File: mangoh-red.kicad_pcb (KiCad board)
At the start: 6 copper layers, 70 x 61.8 mm, 256 parts, among them CN301 uFL, CN302 uFL, CN303 uFL, CN304 USB_A, CN305 USB_B_Micro, CN307 Conn_02x13_Odd_Even, CN312 Conn_02x03_Odd_Even, CN801 USB_B_Micro, CN802 Conn_01x02, CN804 Conn_01x03, J200 CF3-Socket, Q312 NSBC114YDP6T5G, Q400 NSBC114YDP6T5G, Q600 PDTC115EM, SW401 Conn_02x08_Counter_Clockwise, U1004 SX1509BIULTRT, U1005 TPS61253YFFR, U1007 24AA32AF-I-MNY, U301 FT230XQ-R, U306 FXMA108BQX, U307 FXMA108BQX, U400 NCP303LSN30T1G, U402 74AUP1G08GM, U404 TCA9546APWR, U600 XC6223H29B9R-G, U610 TXS02612ZQSR, U701 USB3503A-1-GL-TR, U702 MIC2026-1YM, U704 BMI160, U800 BQ24296RGER, U801 LTC2942IDCB_TRMPBF, U901 TPS62420DRC, U903 XC6221A182MR

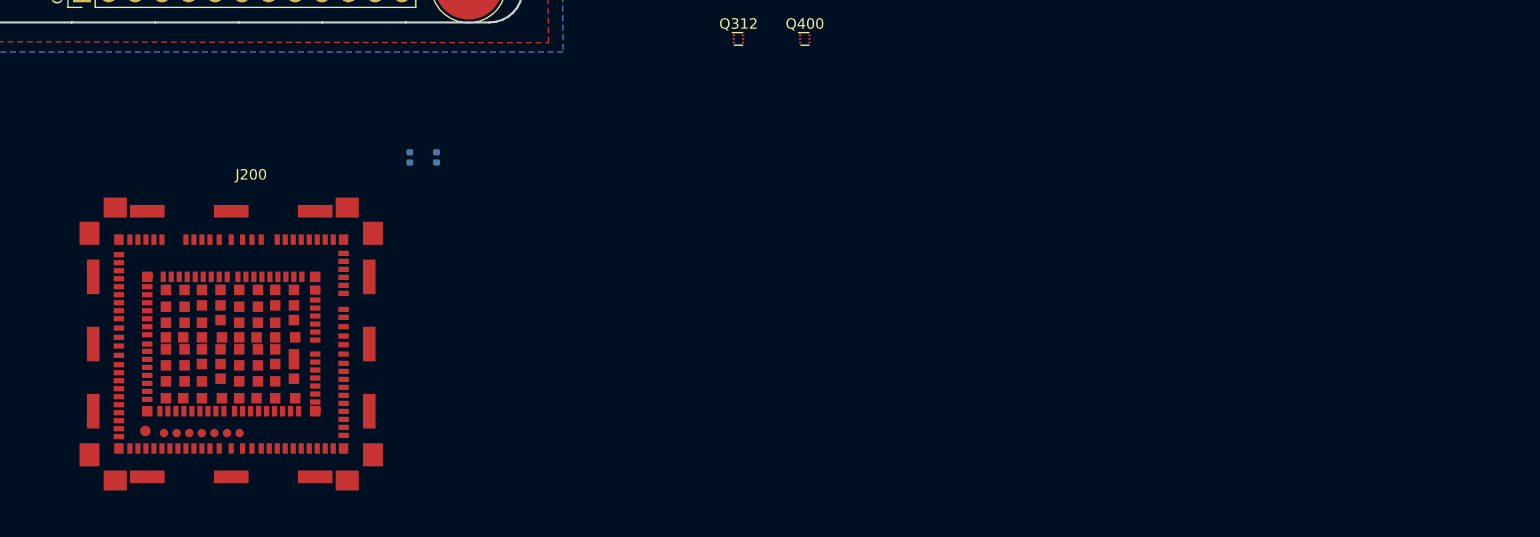
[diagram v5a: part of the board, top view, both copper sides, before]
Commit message: Change footprint of CF3 socket to use the one generated by SnapEDA.
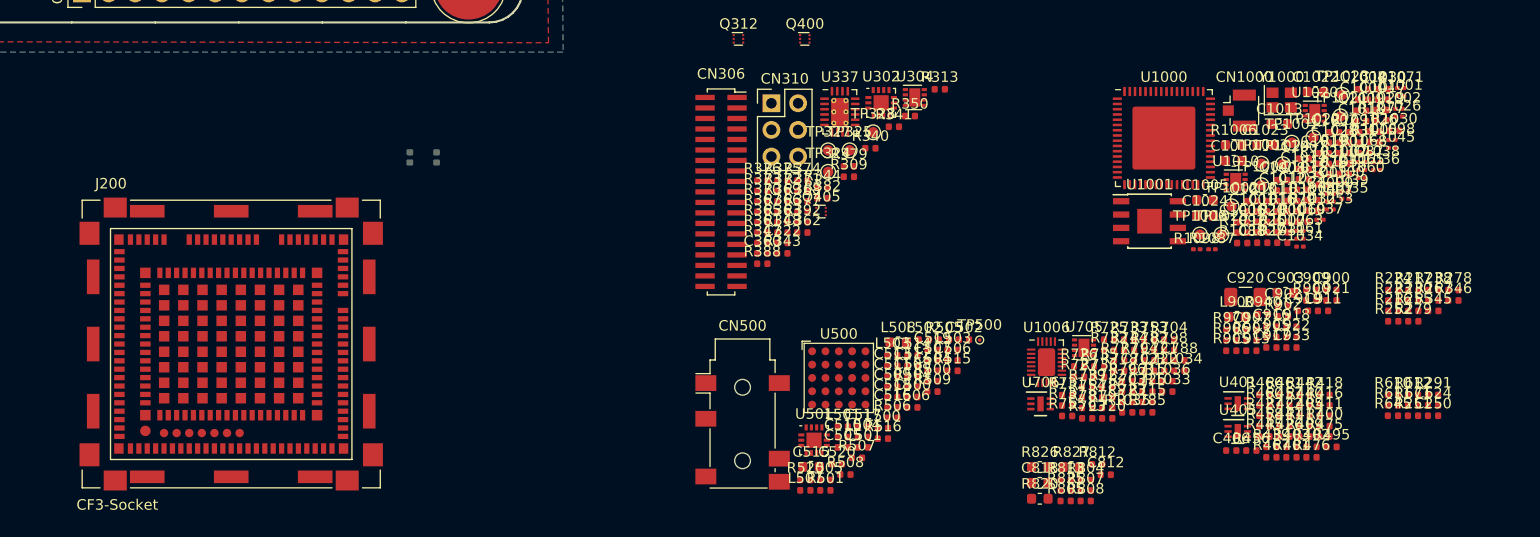
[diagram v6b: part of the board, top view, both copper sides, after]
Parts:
- added C1000: 100n, Capacitor_SMD:C_0402_1005Metric, F.Cu at (269.9, 124.7)
- added C1001: 470n, Capacitor_SMD:C_0402_1005Metric, F.Cu at (259.3, 135.3)
- added C1002: 10p, Capacitor_SMD:C_0402_1005Metric, F.Cu at (267.1, 127.8)
- added C1003: 100n, Capacitor_SMD:C_0402_1005Metric, F.Cu at (259.3, 134.3)
- added C1004: 470n, Capacitor_SMD:C_0402_1005Metric, F.Cu at (269.9, 123.7)
- added C1005: 10u, Capacitor_SMD:C_0603_1608Metric, F.Cu at (254.8, 134.2)
- added C1006: 100p, Capacitor_SMD:C_0402_1005Metric, F.Cu at (258.4, 136.4)
- added C1007: 100n, Capacitor_SMD:C_0402_1005Metric, F.Cu at (264.2, 130.3)
- added C1008: 4.7u, Capacitor_SMD:C_0402_1005Metric, F.Cu at (262.2, 132.3)
- added C1009: 4.7u, Capacitor_SMD:C_0402_1005Metric, F.Cu at (269.7, 125.7)
- added C1010: 2.2u, Capacitor_SMD:C_0603_1608Metric, F.Cu at (257.6, 130.5)
- added C1011: 1u, Capacitor_SMD:C_0402_1005Metric, F.Cu at (261.2, 134.3)
- added C1012: 100n, Capacitor_SMD:C_0402_1005Metric, F.Cu at (262.2, 133.3)
- added C1013: 10u, Capacitor_SMD:C_0603_1608Metric, F.Cu at (261.9, 127.0)
- added C1014: 100n, Capacitor_SMD:C_0402_1005Metric, F.Cu at (264.2, 131.3)
- added C1015: 470p, Capacitor_SMD:C_0402_1005Metric, F.Cu at (264.2, 132.3)
- added C1016: 1u, Capacitor_SMD:C_0402_1005Metric, F.Cu at (261.2, 135.3)
- added C1017: 10u, Capacitor_SMD:C_0402_1005Metric, F.Cu at (271.8, 124.7)
- added C1018: 1u, Capacitor_SMD:C_0402_1005Metric, F.Cu at (269.7, 126.7)
- added C1019: 100p, Capacitor_SMD:C_0402_1005Metric, F.Cu at (266.1, 129.8)
- added C1020: 100n, Capacitor_SMD:C_0402_1005Metric, F.Cu at (260.3, 136.3)
- added C1021: 1u, Capacitor_SMD:C_0402_1005Metric, F.Cu at (266.1, 130.8)
- added C1022: 2.2u, Capacitor_SMD:C_0603_1608Metric, F.Cu at (265.4, 123.9)
- added C1023: 2.2u, Capacitor_SMD:C_0603_1608Metric, F.Cu at (260.6, 129.0)
- added C1024: 2.2u, Capacitor_SMD:C_0603_1608Metric, F.Cu at (254.8, 135.7)
- added C1025: 4.7u, Capacitor_SMD:C_0402_1005Metric, F.Cu at (260.3, 137.3)
- added C1026: 100p, Capacitor_SMD:C_0402_1005Metric, F.Cu at (270.9, 127.7)
- added C1027: 10p, Capacitor_SMD:C_0402_1005Metric, F.Cu at (260.3, 138.3)
- added C1028: 10p, Capacitor_SMD:C_0402_1005Metric, F.Cu at (267.1, 128.8)
- added C1029: 10p, Capacitor_SMD:C_0402_1005Metric, F.Cu at (271.6, 125.7)
- added C1030: 100p, Capacitor_SMD:C_0402_1005Metric, F.Cu at (271.8, 123.7)
- added C1031: 10p, Capacitor_SMD:C_0402_1005Metric, F.Cu at (269.0, 128.8)
- added C1032: 1u, Capacitor_SMD:C_0402_1005Metric, F.Cu at (264.1, 133.3)
- added C1033: 100p, Capacitor_SMD:C_0402_1005Metric, F.Cu at (263.1, 134.3)
- added C1034: 1p, Capacitor_SMD:C_0201_0603Metric, F.Cu at (263.9, 138.7)
- added C1035: 1.5p, Capacitor_SMD:C_0201_0603Metric, F.Cu at (268.2, 134.1)
- added C1036: 1.5p, Capacitor_SMD:C_0201_0603Metric, F.Cu at (271.2, 131.4)
- added C1037: 1.8p, Capacitor_SMD:C_0201_0603Metric, F.Cu at (265.8, 136.1)
- added C1038: 1.8p, Capacitor_SMD:C_0201_0603Metric, F.Cu at (271.2, 130.6)
- added C1039: 1.5p, Capacitor_SMD:C_0201_0603Metric, F.Cu at (268.2, 133.4)
- added C1045: 10p, Capacitor_SMD:C_0201_0603Metric, F.Cu at (272.6, 129.3)
- added C1053: 1.5p, Capacitor_SMD:C_0201_0603Metric, F.Cu at (266.7, 135.1)
- added C1060: 2.7p, Capacitor_SMD:C_0201_0603Metric, F.Cu at (269.7, 132.1)
- added C1061: 100p, Capacitor_SMD:C_0201_0603Metric, F.Cu at (263.9, 137.9)
- added C1063: 10p, Capacitor_SMD:C_0201_0603Metric, F.Cu at (263.9, 137.2)
- added C1065: 1.5p, Capacitor_SMD:C_0201_0603Metric, F.Cu at (269.7, 131.4)
- added C1087: 2.2p, Capacitor_SMD:C_0201_0603Metric, F.Cu at (266.7, 134.4)
- added C1098: 10p, Capacitor_SMD:C_0201_0603Metric, F.Cu at (272.6, 128.5)
- added C1099: 10p, Capacitor_SMD:C_0201_0603Metric, F.Cu at (266.7, 133.6)
- added C1100: 10p, Capacitor_SMD:C_0201_0603Metric, F.Cu at (267.8, 132.6)
- added C250: 1n, Capacitor_SMD:C_0402_1005Metric, F.Cu at (276.5, 154.8)
- added C322: 100n, Capacitor_SMD:C_0402_1005Metric, F.Cu at (214.6, 138.3)
- added C360: 100n, Capacitor_SMD:C_0402_1005Metric, F.Cu at (212.6, 139.3)
- added C362: 100n, Capacitor_SMD:C_0402_1005Metric, F.Cu at (216.5, 137.3)
- added C405: 100n, Capacitor_SMD:C_0402_1005Metric, F.Cu at (264.3, 154.8)
- added C406: 100n, Capacitor_SMD:C_0402_1005Metric, F.Cu at (257.3, 158.1)
- added C500: 100p, Capacitor_SMD:C_0402_1005Metric, F.Cu at (226.9, 153.0)
- added C501: 100p, Capacitor_SMD:C_0402_1005Metric, F.Cu at (222.2, 157.8)
- added C502: 100p, Capacitor_SMD:C_0402_1005Metric, F.Cu at (231.9, 147.5)
- added C503: 1u, Capacitor_SMD:C_0402_1005Metric, F.Cu at (230.8, 148.5)
- added C504: 1u, Capacitor_SMD:C_0402_1005Metric, F.Cu at (228.9, 150.5)
- added C505: 100p, Capacitor_SMD:C_0402_1005Metric, F.Cu at (220.3, 157.8)
- added C506: 100p, Capacitor_SMD:C_0402_1005Metric, F.Cu at (230.8, 149.5)
- added C507: 22p, Capacitor_SMD:C_0402_1005Metric, F.Cu at (228.9, 149.5)
- added C508: 22p, Capacitor_SMD:C_0402_1005Metric, F.Cu at (226.9, 151.0)
- added C509: 4.7u, Capacitor_SMD:C_0402_1005Metric, F.Cu at (225.0, 152.0)
- added C510: 100p, Capacitor_SMD:C_0402_1005Metric, F.Cu at (220.3, 156.8)
- added C511: 100p, Capacitor_SMD:C_0402_1005Metric, F.Cu at (225.0, 151.0)
- added C512: 4.7u, Capacitor_SMD:C_0402_1005Metric, F.Cu at (226.9, 150.0)
- added C513: 4.7u, Capacitor_SMD:C_0402_1005Metric, F.Cu at (225.0, 150.0)
- added C514: 4.7u, Capacitor_SMD:C_0402_1005Metric, F.Cu at (226.9, 149.0)
- added C515: 2.2u, Capacitor_SMD:C_0603_1608Metric, F.Cu at (217.3, 159.7)
- added C516: 100p, Capacitor_SMD:C_0402_1005Metric, F.Cu at (225.0, 154.0)
- added C517: 100n, Capacitor_SMD:C_0402_1005Metric, F.Cu at (222.2, 155.8)
- added C518: 100n, Capacitor_SMD:C_0402_1005Metric, F.Cu at (225.0, 153.0)
- added C519: 4.7u, Capacitor_SMD:C_0402_1005Metric, F.Cu at (228.9, 148.5)
- added C520: 100n, Capacitor_SMD:C_0402_1005Metric, F.Cu at (219.8, 159.4)
- added C624: 100n, Capacitor_SMD:C_0402_1005Metric, F.Cu at (276.5, 153.8)
- added C702: 100n, Capacitor_SMD:C_0402_1005Metric, F.Cu at (248.6, 150.5)
- added C715: 100n, Capacitor_SMD:C_0402_1005Metric, F.Cu at (249.3, 151.5)
- added C720: 100n, Capacitor_SMD:C_0402_1005Metric, F.Cu at (245.5, 155.0)
- added C721: 100n, Capacitor_SMD:C_0402_1005Metric, F.Cu at (250.5, 149.5)
- added C722: 100n, Capacitor_SMD:C_0402_1005Metric, F.Cu at (250.5, 150.5)
- added C723: 100n, Capacitor_SMD:C_0402_1005Metric, F.Cu at (247.4, 153.5)
- added C725: 100n, Capacitor_SMD:C_0402_1005Metric, F.Cu at (249.3, 152.5)
- added C788: 4.7u, Capacitor_SMD:C_0402_1005Metric, F.Cu at (252.4, 149.5)
- added C812: 10u, Capacitor_SMD:C_0402_1005Metric, F.Cu at (245.4, 160.4)
- added C818: 10u, Capacitor_SMD:C_0603_1608Metric, F.Cu at (239.1, 161.2)
- added C900: 100n, Capacitor_SMD:C_0402_1005Metric, F.Cu at (266.9, 142.8)
- added C902: 100n, Capacitor_SMD:C_0402_1005Metric, F.Cu at (262.2, 144.3)
- added C903: 10u, Capacitor_SMD:C_0603_1608Metric, F.Cu at (262.5, 143.1)
- added C905: 100n, Capacitor_SMD:C_0402_1005Metric, F.Cu at (261.1, 147.3)
- added C907: 100n, Capacitor_SMD:C_0402_1005Metric, F.Cu at (259.2, 146.6)
- added C909: 47n, Capacitor_SMD:C_0402_1005Metric, F.Cu at (264.9, 142.8)
- added C911: 10n, Capacitor_SMD:C_0402_1005Metric, F.Cu at (266.1, 144.8)
- added C915: 100n, Capacitor_SMD:C_0402_1005Metric, F.Cu at (259.2, 148.6)
- added C916: 100n, Capacitor_SMD:C_0402_1005Metric, F.Cu at (261.1, 146.3)
- added C917: 100n, Capacitor_SMD:C_0402_1005Metric, F.Cu at (261.1, 148.3)
- added C918: 100n, Capacitor_SMD:C_0402_1005Metric, F.Cu at (263.1, 146.3)
- added C919: 100n, Capacitor_SMD:C_0402_1005Metric, F.Cu at (264.2, 144.8)
- added C920: 47u, Capacitor_SMD:C_1206_3216Metric, F.Cu at (258.7, 143.5)
- added C921: 100n, Capacitor_SMD:C_0402_1005Metric, F.Cu at (266.9, 143.8)
- added C922: 1.5m, Capacitor_SMD:C_0402_1005Metric, F.Cu at (263.1, 147.3)
- added C933: 100n, Capacitor_SMD:C_0402_1005Metric, F.Cu at (263.1, 148.3)
- added CN1000: uFL, Connector_Coaxial:U.FL_Hirose_U.FL-R-SMT-1_Vertical, F.Cu at (258.1, 125.7)
- added CN306: Conn_02x19_Counter_Clockwise, Connector_PinSocket_1.00mm:PinSocket_2x19_P1.00mm_Vertical_SMD, F.Cu at (208.7, 133.5)
- added CN310: Conn_02x03_Odd_Even, Connector_PinHeader_2.54mm:PinHeader_2x03_P2.54mm_Vertical, F.Cu at (213.5, 125.0)
- added CN500: JP036-RT3B4AB, Connector_Audio:Jack_3.5mm_PJ311_Horizontal, F.Cu at (210.8, 156.4)
- added L1001: 1.2n, Inductor_SMD:L_0201_0603Metric, F.Cu at (273.5, 124.3)
- added L1002: 1.2n, Inductor_SMD:L_0201_0603Metric, F.Cu at (273.3, 125.5)
- added L1026: 2.2n, Inductor_SMD:L_0201_0603Metric, F.Cu at (273.3, 126.3)
- added L1087: 2.4n, Inductor_SMD:L_0201_0603Metric, F.Cu at (269.7, 130.6)
- added L500: 0, Inductor_SMD:L_0402_1005Metric, F.Cu at (224.1, 156.0)
- added L501: 0, Inductor_SMD:L_0402_1005Metric, F.Cu at (220.3, 155.8)
- added L502: 22n, Inductor_SMD:L_0402_1005Metric, F.Cu at (228.0, 147.5)
- added L503: 22n, Inductor_SMD:L_0402_1005Metric, F.Cu at (225.0, 149.0)
- added L504: 0, Inductor_SMD:L_0402_1005Metric, F.Cu at (222.2, 156.8)
- added L505: 0, Inductor_SMD:L_0402_1005Metric, F.Cu at (218.7, 160.9)
- added L506: 0, Inductor_SMD:L_0402_1005Metric, F.Cu at (226.9, 154.0)
- added L507: 0, Inductor_SMD:L_0402_1005Metric, F.Cu at (216.7, 161.9)
- added L508: 0, Inductor_SMD:L_0603_1608Metric, F.Cu at (225.6, 147.8)
- added L900: 0, Inductor_SMD:L_0603_1608Metric, F.Cu at (257.9, 145.4)
- added Q405: NSBC114YDP6T5G, MangOH-Red:SOT963_6P_0100x0080_0035CC, F.Cu at (218.2, 135.3)
- added R1000: 10k, Resistor_SMD:R_0402_1005Metric, F.Cu at (262.2, 136.3)
- added R1001: 10k, Resistor_SMD:R_0402_1005Metric, F.Cu at (268.0, 129.8)
- added R1002: 10k, Resistor_SMD:R_0402_1005Metric, F.Cu at (268.0, 130.8)
- added R1003: 10k, Resistor_SMD:R_0402_1005Metric, F.Cu at (266.1, 132.8)
- added R1004: 10k, Resistor_SMD:R_0402_1005Metric, F.Cu at (265.1, 134.3)
- added R1005: 10k, Resistor_SMD:R_0402_1005Metric, F.Cu at (270.9, 128.7)
- added R1006: 0, Resistor_SMD:R_0603_1608Metric, F.Cu at (257.6, 129.0)
- added R1007: 36, Resistor_SMD:R_0402_1005Metric, F.Cu at (262.2, 137.3)
- added R1030: 10K, Resistor_SMD:R_0402_1005Metric, F.Cu at (272.9, 127.6)
- added R1031: 10K, Resistor_SMD:R_0402_1005Metric, F.Cu at (262.2, 138.3)
- added R1032: 10K, Resistor_SMD:R_0402_1005Metric, F.Cu at (265.1, 135.2)
- added R1033: 47k, Resistor_SMD:R_0402_1005Metric, F.Cu at (251.2, 152.5)
- added R1034: 47k, Resistor_SMD:R_0402_1005Metric, F.Cu at (252.4, 150.5)
- added R1035: 33, Resistor_SMD:R_0402_1005Metric, F.Cu at (247.4, 154.5)
- added R1036: 33, Resistor_SMD:R_0402_1005Metric, F.Cu at (251.2, 151.5)
- added R1051: 10k, Resistor_SMD:R_0402_1005Metric, F.Cu at (268.0, 131.7)
- added R1068: 0, Resistor_SMD:R_0402_1005Metric, F.Cu at (270.0, 129.8)
- added R1069: 10K, Resistor_SMD:R_0402_1005Metric, F.Cu at (264.1, 136.3)
- added R1071: 10k, Resistor_SMD:R_0201_0603Metric, F.Cu at (273.5, 123.6)
- added R1077: 10k, Resistor_SMD:R_0402_1005Metric, F.Cu at (271.6, 126.7)
- added R1078: 0, Resistor_SMD:R_0402_1005Metric, F.Cu at (266.1, 131.8)
- added R1079: 10k, Resistor_SMD:R_0402_1005Metric, F.Cu at (263.1, 135.3)
- added R1087: 10k, Resistor_SMD:R_0201_0603Metric, F.Cu at (255.5, 138.9)
- added R1088: 10k, Resistor_SMD:R_0402_1005Metric, F.Cu at (258.4, 138.3)
- added R1091: 0, Resistor_SMD:R_0402_1005Metric, F.Cu at (269.0, 127.8)
- added R1092: 0, Resistor_SMD:R_0402_1005Metric, F.Cu at (258.4, 137.3)
- added R1098: 2.7p, Resistor_SMD:R_0201_0603Metric, F.Cu at (254.0, 138.9)
- added R216: 0, Resistor_SMD:R_0402_1005Metric, F.Cu at (272.8, 144.8)
- added R217: 0, Resistor_SMD:R_0402_1005Metric, F.Cu at (274.7, 142.8)
- added R223: 0, Resistor_SMD:R_0402_1005Metric, F.Cu at (272.8, 143.8)
- added R224: 0, Resistor_SMD:R_0402_1005Metric, F.Cu at (272.8, 142.8)
- added R230: 0, Resistor_SMD:R_0402_1005Metric, F.Cu at (274.7, 143.8)
- added R238: 0, Resistor_SMD:R_0402_1005Metric, F.Cu at (276.6, 142.8)
- added R251: 100k, Resistor_SMD:R_0402_1005Metric, F.Cu at (274.6, 154.8)
- added R252: 0, Resistor_SMD:R_0402_1005Metric, F.Cu at (272.8, 145.8)
- added R255: 0, Resistor_SMD:R_0402_1005Metric, F.Cu at (274.7, 144.8)
- added R267: 0, Resistor_SMD:R_0402_1005Metric, F.Cu at (276.6, 143.8)
- added R278: 0, Resistor_SMD:R_0402_1005Metric, F.Cu at (278.5, 142.8)
- added R279: 0, Resistor_SMD:R_0402_1005Metric, F.Cu at (274.7, 145.8)
- added R291: 100k, Resistor_SMD:R_0402_1005Metric, F.Cu at (276.5, 152.8)
- added R309: 0, Resistor_SMD:R_0402_1005Metric, F.Cu at (220.9, 132.0)
- added R313: 10k, Resistor_SMD:R_0402_1005Metric, F.Cu at (229.6, 123.7)
- added R340: 0, Resistor_SMD:R_0402_1005Metric, F.Cu at (222.9, 129.3)
- added R341: 0, Resistor_SMD:R_0402_1005Metric, F.Cu at (225.2, 127.3)
- added R343: 0, Resistor_SMD:R_0402_1005Metric, F.Cu at (214.6, 139.3)
- added R344: 0, Resistor_SMD:R_0402_1005Metric, F.Cu at (218.4, 133.1)
- added R345: 0, Resistor_SMD:R_0402_1005Metric, F.Cu at (276.6, 144.8)
- added R346: 0, Resistor_SMD:R_0402_1005Metric, F.Cu at (278.5, 143.8)
- added R347: 0, Resistor_SMD:R_0402_1005Metric, F.Cu at (212.6, 138.3)
- added R348: 0, Resistor_SMD:R_0402_1005Metric, F.Cu at (214.6, 137.3)
- added R350: 0, Resistor_SMD:R_0402_1005Metric, F.Cu at (226.7, 126.2)
- added R361: 820k, Resistor_SMD:R_0402_1005Metric, F.Cu at (212.6, 137.3)
- added R363: 0, Resistor_SMD:R_0402_1005Metric, F.Cu at (214.6, 136.3)
- added R365: 0, Resistor_SMD:R_0402_1005Metric, F.Cu at (212.6, 136.3)
- added R366: 0, Resistor_SMD:R_0402_1005Metric, F.Cu at (214.6, 135.4)
- added R367: 0, Resistor_SMD:R_0402_1005Metric, F.Cu at (212.6, 135.4)
- added R368: 0, Resistor_SMD:R_0402_1005Metric, F.Cu at (216.5, 134.4)
- added R369: 0, Resistor_SMD:R_0402_1005Metric, F.Cu at (214.6, 134.4)
- added R370: 0, Resistor_SMD:R_0402_1005Metric, F.Cu at (212.6, 134.4)
- added R371: 0, Resistor_SMD:R_0402_1005Metric, F.Cu at (216.5, 133.4)
- added R372: 10k, Resistor_SMD:R_0402_1005Metric, F.Cu at (214.6, 133.4)
- added R373: 0, Resistor_SMD:R_0402_1005Metric, F.Cu at (212.6, 133.4)
- added R374: 0, Resistor_SMD:R_0402_1005Metric, F.Cu at (216.5, 132.4)
- added R375: 0, Resistor_SMD:R_0402_1005Metric, F.Cu at (214.6, 132.4)
- added R376: 10k, Resistor_SMD:R_0402_1005Metric, F.Cu at (212.6, 132.4)
- added R377: 10k, Resistor_SMD:R_0402_1005Metric, F.Cu at (216.5, 135.4)
- added R379: 10k, Resistor_SMD:R_0402_1005Metric, F.Cu at (220.9, 131.0)
- added R382: 0, Resistor_SMD:R_0402_1005Metric, F.Cu at (218.4, 134.1)
- added R388: 10k, Resistor_SMD:R_0402_1005Metric, F.Cu at (212.6, 140.3)
- added R392: 0, Resistor_SMD:R_0402_1005Metric, F.Cu at (216.5, 136.3)
- added R400: 0, Resistor_SMD:R_0402_1005Metric, F.Cu at (266.2, 155.8)
- added R401: 47k, Resistor_SMD:R_0402_1005Metric, F.Cu at (263.1, 158.7)
- added R402: 100k, Resistor_SMD:R_0402_1005Metric, F.Cu at (265.0, 157.8)
- added R403: 47k, Resistor_SMD:R_0402_1005Metric, F.Cu at (263.1, 157.8)
- added R409: 330, Resistor_SMD:R_0402_1005Metric, F.Cu at (264.3, 156.8)
- added R411: 10k, Resistor_SMD:R_0402_1005Metric, F.Cu at (266.2, 154.8)
- added R416: 0, Resistor_SMD:R_0402_1005Metric, F.Cu at (266.2, 153.8)
- added R417: 0, Resistor_SMD:R_0402_1005Metric, F.Cu at (264.3, 155.8)
- added R418: 0, Resistor_SMD:R_0402_1005Metric, F.Cu at (266.2, 152.8)
- added R422: 10k, Resistor_SMD:R_0402_1005Metric, F.Cu at (262.4, 154.8)
- added R426: 0, Resistor_SMD:R_0402_1005Metric, F.Cu at (262.4, 156.8)
- added R427: 0, Resistor_SMD:R_0402_1005Metric, F.Cu at (260.5, 154.8)
- added R439: 0, Resistor_SMD:R_0402_1005Metric, F.Cu at (261.1, 157.8)
- added R440: 0, Resistor_SMD:R_0402_1005Metric, F.Cu at (264.3, 153.8)
- added R441: 0, Resistor_SMD:R_0402_1005Metric, F.Cu at (262.4, 155.8)
- added R442: 0, Resistor_SMD:R_0402_1005Metric, F.Cu at (264.3, 152.8)
- added R445: 100, Resistor_SMD:R_0402_1005Metric, F.Cu at (260.5, 156.8)
- added R456: 47k, Resistor_SMD:R_0402_1005Metric, F.Cu at (259.2, 158.1)
- added R457: 47k, Resistor_SMD:R_0402_1005Metric, F.Cu at (262.4, 153.8)
- added R458: 330, Resistor_SMD:R_0402_1005Metric, F.Cu at (260.5, 155.8)
- added R460: 0, Resistor_SMD:R_0402_1005Metric, F.Cu at (260.5, 153.8)
- added R461: 0, Resistor_SMD:R_0402_1005Metric, F.Cu at (262.4, 152.8)
- added R466: 4.7k, Resistor_SMD:R_0402_1005Metric, F.Cu at (260.5, 152.8)
- added R467: 0, Resistor_SMD:R_0402_1005Metric, F.Cu at (261.1, 158.7)
- added R475: 0, Resistor_SMD:R_0402_1005Metric, F.Cu at (266.2, 156.8)
- added R476: 47k, Resistor_SMD:R_0402_1005Metric, F.Cu at (265.0, 158.7)
- added R495: 0, Resistor_SMD:R_0402_1005Metric, F.Cu at (266.9, 157.8)
- added R500: 2.2k, Resistor_SMD:R_0402_1005Metric, F.Cu at (228.9, 151.5)
- added R501: 2.2k, Resistor_SMD:R_0402_1005Metric, F.Cu at (218.7, 161.9)
- added R504: 20K, Resistor_SMD:R_0402_1005Metric, F.Cu at (226.9, 152.0)
- added R505: 0, Resistor_SMD:R_0402_1005Metric, F.Cu at (230.0, 147.5)
- added R506: 0, Resistor_SMD:R_0402_1005Metric, F.Cu at (225.0, 155.0)
- added R507: 0, Resistor_SMD:R_0402_1005Metric, F.Cu at (221.7, 158.8)
- added R508: 10k, Resistor_SMD:R_0402_1005Metric, F.Cu at (220.6, 160.4)
- added R509: 10k, Resistor_SMD:R_0402_1005Metric, F.Cu at (228.9, 152.5)
- added R515: 0, Resistor_SMD:R_0402_1005Metric, F.Cu at (230.8, 150.5)
- added R516: 0, Resistor_SMD:R_0402_1005Metric, F.Cu at (224.1, 157.0)
- added R520: 10k, Resistor_SMD:R_0402_1005Metric, F.Cu at (216.7, 160.9)
- added R610: 0, Resistor_SMD:R_0402_1005Metric, F.Cu at (272.7, 152.8)
- added R611: 0, Resistor_SMD:R_0402_1005Metric, F.Cu at (272.7, 153.8)
- added R612: 0, Resistor_SMD:R_0402_1005Metric, F.Cu at (274.6, 152.8)
- added R645: 0, Resistor_SMD:R_0402_1005Metric, F.Cu at (272.7, 154.8)
- added R671: 10k, Resistor_SMD:R_0402_1005Metric, F.Cu at (274.6, 153.8)
- added R703: 10k, Resistor_SMD:R_0402_1005Metric, F.Cu at (247.4, 152.5)
- added R704: 10k, Resistor_SMD:R_0402_1005Metric, F.Cu at (251.4, 147.5)
- added R715: 10k, Resistor_SMD:R_0402_1005Metric, F.Cu at (249.3, 153.5)
- added R722: 10k, Resistor_SMD:R_0402_1005Metric, F.Cu at (245.5, 152.1)
- added R725: 0, Resistor_SMD:R_0402_1005Metric, F.Cu at (245.7, 147.5)
- added R726: 10k, Resistor_SMD:R_0402_1005Metric, F.Cu at (242.8, 150.1)
- added R727: 10k, Resistor_SMD:R_0402_1005Metric, F.Cu at (242.8, 151.1)
- added R731: 10k, Resistor_SMD:R_0402_1005Metric, F.Cu at (241.7, 152.8)
- added R732: 0, Resistor_SMD:R_0402_1005Metric, F.Cu at (245.7, 148.5)
- added R733: 0, Resistor_SMD:R_0402_1005Metric, F.Cu at (247.6, 147.5)
- added R735: 10K, Resistor_SMD:R_0402_1005Metric, F.Cu at (244.7, 150.1)
- added R736: 0, Resistor_SMD:R_0402_1005Metric, F.Cu at (244.7, 151.1)
- added R737: 0, Resistor_SMD:R_0402_1005Metric, F.Cu at (241.7, 153.8)
- added R739: 0, Resistor_SMD:R_0402_1005Metric, F.Cu at (243.6, 152.1)
- added R744: 10k, Resistor_SMD:R_0402_1005Metric, F.Cu at (247.6, 148.5)
- added R753: 0, Resistor_SMD:R_0402_1005Metric, F.Cu at (249.5, 147.5)
- added R754: 0, Resistor_SMD:R_0402_1005Metric, F.Cu at (243.6, 153.1)
- added R755: 0, Resistor_SMD:R_0402_1005Metric, F.Cu at (241.7, 154.8)
- added R777: 10k, Resistor_SMD:R_0402_1005Metric, F.Cu at (246.6, 149.5)
- added R778: 0, Resistor_SMD:R_0402_1005Metric, F.Cu at (246.6, 150.5)
- added R781: 10k, Resistor_SMD:R_0402_1005Metric, F.Cu at (243.6, 154.0)
- added R782: 0, Resistor_SMD:R_0402_1005Metric, F.Cu at (249.5, 148.5)
- added R785: 0, Resistor_SMD:R_0402_1005Metric, F.Cu at (249.3, 154.5)
- added R786: 0, Resistor_SMD:R_0402_1005Metric, F.Cu at (245.5, 153.1)
- added R793: 0, Resistor_SMD:R_0402_1005Metric, F.Cu at (243.6, 155.0)
- added R794: 0, Resistor_SMD:R_0402_1005Metric, F.Cu at (248.6, 149.5)
- added R795: 0, Resistor_SMD:R_0402_1005Metric, F.Cu at (245.5, 154.0)
- added R796: 0, Resistor_SMD:R_0402_1005Metric, F.Cu at (247.4, 151.5)
- added R798: 0, Resistor_SMD:R_0402_1005Metric, F.Cu at (251.4, 148.5)
- added R804: 10k, Resistor_SMD:R_0402_1005Metric, F.Cu at (243.5, 160.9)
- added R805: 10k, Resistor_SMD:R_0402_1005Metric, F.Cu at (241.5, 162.9)
- added R807: 10k, Resistor_SMD:R_0402_1005Metric, F.Cu at (243.5, 161.9)
- added R808: 10k, Resistor_SMD:R_0402_1005Metric, F.Cu at (243.5, 162.9)
- added R812: 10k, Resistor_SMD:R_0402_1005Metric, F.Cu at (244.6, 159.4)
- added R813: 15k, Resistor_SMD:R_0402_1005Metric, F.Cu at (241.5, 160.9)
- added R820: 0, Resistor_SMD:R_0603_1608Metric, F.Cu at (239.1, 162.7)
- added R825: 0, Resistor_SMD:R_0402_1005Metric, F.Cu at (241.5, 161.9)
- added R826: 0, Resistor_SMD:R_0603_1608Metric, F.Cu at (239.1, 159.7)
- added R827: 0, Resistor_SMD:R_0603_1608Metric, F.Cu at (242.1, 159.7)
- added R900: 33k, Resistor_SMD:R_0402_1005Metric, F.Cu at (264.9, 143.8)
- added R902: 0, Resistor_SMD:R_0402_1005Metric, F.Cu at (262.2, 145.3)
- added R903: 0, Resistor_SMD:R_0402_1005Metric, F.Cu at (259.2, 147.6)
- added R905: 220k, Resistor_SMD:R_0402_1005Metric, F.Cu at (257.3, 148.6)
- added R906: 33k, Resistor_SMD:R_0402_1005Metric, F.Cu at (257.3, 147.6)
- added R940: 0, Resistor_SMD:R_0402_1005Metric, F.Cu at (260.3, 145.1)
- added R970: 0, Resistor_SMD:R_0402_1005Metric, F.Cu at (257.3, 146.6)
- added TP1000: TestPoint, MangOH-Red:Test_Point_Pad_d_0100, F.Cu at (254.3, 137.5)
- added TP1001: TestPoint, MangOH-Red:Test_Point_Pad_d_0100, F.Cu at (263.1, 128.8)
- added TP1002: TestPoint, MangOH-Red:Test_Point_Pad_d_0100, F.Cu at (257.3, 134.8)
- added TP1003: TestPoint, MangOH-Red:Test_Point_Pad_d_0100, F.Cu at (260.2, 130.8)
- added TP1004: TestPoint, MangOH-Red:Test_Point_Pad_d_0100, F.Cu at (260.2, 132.8)
- added TP1021: TestPoint, MangOH-Red:Test_Point_Pad_d_0100, F.Cu at (267.7, 126.3)
- added TP1022: TestPoint, MangOH-Red:Test_Point_Pad_d_0100, F.Cu at (265.1, 128.3)
- added TP1023: TestPoint, MangOH-Red:Test_Point_Pad_d_0100, F.Cu at (267.9, 124.2)
- added TP1024: TestPoint, MangOH-Red:Test_Point_Pad_d_0100, F.Cu at (262.2, 130.8)
- added TP1025: TestPoint, MangOH-Red:Test_Point_Pad_d_0100, F.Cu at (256.4, 137.5)
- added TP324: TestPoint, MangOH-Red:Test_Point_Pad_d_0100, F.Cu at (218.9, 131.6)
- added TP325: TestPoint, MangOH-Red:Test_Point_Pad_d_0100, F.Cu at (221.0, 129.5)
- added TP327: TestPoint, MangOH-Red:Test_Point_Pad_d_0100, F.Cu at (218.9, 129.5)
- added TP328: TestPoint, MangOH-Red:Test_Point_Pad_d_0100, F.Cu at (223.2, 127.8)
- added TP500: TestPoint, MangOH-Red:Test_Point_Pad_d_0035, F.Cu at (233.4, 147.6)
- added U1000: MT7697, MangOH-Red:QFN_68P_0800x0800_SLUG_0550x0550_0040CC, F.Cu at (250.9, 128.3)
- added U1001: MX25L3233FM1I-08G_TR, MangOH-Red:SOIC_8P_0490x0390_0127CC, F.Cu at (249.5, 136.3)
- added U1006: CP2130-F01-GM, MangOH-Red:QFN_24P_0400x0400_SLUG_0270x0270_0050CC, F.Cu at (239.7, 149.7)
- added U1010: 74LVC2G126HD4-7, MangOH-Red:DFN_8P_0200x0100_0050CC, F.Cu at (257.7, 132.5)
- added U1020: 74LVC2G126HD4-7, MangOH-Red:DFN_8P_0200x0100_0050CC, F.Cu at (265.3, 126.0)
- added U302: TS3A5018RSVR, MangOH-Red:QFN_14P_0250x0300_0050CC, F.Cu at (224.0, 125.0)
- added U304: 74LVC2G126HD4-7, MangOH-Red:DFN_8P_0200x0100_0050CC, F.Cu at (227.2, 124.5)
- added U337: FXMA108BQX, MangOH-Red:QFN_20P_0250x0450_SLUG_0115x0315_0050CC, F.Cu at (220.0, 125.8)
- added U401: 74AUP1G08GM, Package_DFN_QFN:DFN-6-1EP_2x2mm_P0.5mm_EP0.61x1.42mm, F.Cu at (257.9, 153.6)
- added U405: 74AUP1G08GM, Package_DFN_QFN:DFN-6-1EP_2x2mm_P0.5mm_EP0.61x1.42mm, F.Cu at (257.9, 156.3)
- added U500: WM8944BECS_R, MangOH-Red:BGA_25P_0241x0241_0050CC_0030PD, F.Cu at (219.9, 151.2)
- added U501: TS3A5018RSVR, MangOH-Red:QFN_14P_0250x0300_0050CC, F.Cu at (217.6, 157.1)
- added U705: BMP280, MangOH-Red:DFN_8P_0250x0200_0065CC, F.Cu at (243.3, 148.3)
- added U706: PNJ4K01F, Package_DFN_QFN:DFN-6-1EP_2x2mm_P0.5mm_EP0.61x1.42mm, F.Cu at (239.2, 153.7)
- added Y1000: CT2520DB26000C0FZZA1, Crystal:Crystal_SMD_2520-4Pin_2.5x2.0mm, F.Cu at (262.1, 124.7)
- J200: footprint MangOH-Red:CF3-Socket -> WP_SNAP-IN_BASE:SIERRA_WP_SNAP-IN_BASE
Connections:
- C400 pad 1: Power_Fail_Indicator -> RESET_IN
- CN307 pad 12: PWM_OUT_3V3 -> Net-(CN307-Pad12)
- CN307 pad 2: VCC -> Net-(CN307-Pad2)
- CN307 pad 3: SDA_EXP -> Net-(CN307-Pad3)
- CN307 pad 4: VCC -> Net-(CN307-Pad2)
- CN307 pad 5: SCL_EXP -> Net-(CN307-Pad5)
- CN312 pad 1: SENSOR_INT1 -> WP_GPIO_4_Wakeable
- CN312 pad 3: SENSOR_INT2 -> WP_GPIO_5_Wakeable
- CN312 pad 4: ADC1 -> Net-(CN312-Pad4)
- CN312 pad 5: ADC2 -> RFU_PIN
- D400 pad 1: Power_Fail_Indicator -> RESET_IN
- Q312 pad 1: (no net) -> GND
- Q312 pad 2: (no net) -> Net-(Q312-Pad2)
- Q312 pad 5: VCC -> Net-(Q312-Pad5)
- Q312 pad 6: (no net) -> Net-(Q312-Pad6)
- Q400 pad 2: BattChrgr_INT_N -> LED_CARD_DETECT_IOT0
- R410 pad 2: Power_Fail_Indicator -> RESET_IN
- R429 pad 2: Charger_I2C_CLK -> Net-(R427-Pad1)
- R431 pad 2: Charger_I2C_DATA -> Net-(R426-Pad1)
- R462 pad 1: GPIO1|I2C1_CLK -> WIFI_I2C0_DATA
- R463 pad 1: GPIO1|I2C1_CLK -> WIFI_I2C0_CLK
- SW401 pad 13: VCC -> Net-(R495-Pad2)
- TP803 pad 1: VCC -> Net-(R827-Pad2)
- U1004 pad 13: BattChrgr_INT_N -> Net-(R785-Pad2)
- U1004 pad 14: SDIO_SEL -> Net-(R755-Pad2)
- U1004 pad 23: System_reset -> GPIO_IOT0_RESET
- U1004 pad 6: MTK_TO_WP_UART_EN -> Net-(R753-Pad2)
- U307 pad 11: GND -> Net-(Q312-Pad6)
- U307 pad 12: /3. RF, USB, IOT connectors/CTS_FTDI -> /3. RF, USB, IOT connectors/UART2_CTS_3V3
- U307 pad 13: /3. RF, USB, IOT connectors/RTS_FTDI -> /3. RF, USB, IOT connectors/UART2_RTS_3V3
- U307 pad 14: /3. RF, USB, IOT connectors/RX_FTDI -> /3. RF, USB, IOT connectors/UART2_RX_3V3
- U307 pad 15: /3. RF, USB, IOT connectors/TX_FTDI -> WIFI_UART0_TX
- U307 pad 17: Net-(U307-Pad17) -> RESET_WIFI_3V3
- U307 pad 4: Net-(U307-Pad4) -> RESET_WIFI_1V8
- U400 pad 1: Power_Fail_Indicator -> Net-(R441-Pad1)
- U400 pad 2: VCC -> Net-(R400-Pad1)
- U402 pad 1: Power_Fail_Indicator -> RESET_IN
- U402 pad 4: System_reset -> GPIO_IOT0_RESET
- U404 pad 1: VCC -> Net-(R417-Pad2)
- U404 pad 13: GND -> Net-(R418-Pad2)
- U404 pad 2: GND -> Net-(R416-Pad2)
- U404 pad 3: System_reset -> Net-(R466-Pad2)
- U404 pad 6: Charger_I2C_CLK -> Net-(R427-Pad1)
- U404 pad 7: Charger_I2C_DATA -> Net-(R426-Pad1)
- U610 pad C4: VCC -> Net-(R610-Pad2)
- U701 pad E3: System_reset -> GPIO_IOT0_RESET
- U702 pad 2: OSC_N -> Net-(R725-Pad2)
- U702 pad 3: OSC_N -> Net-(R725-Pad2)
- U704 pad 13: GPIO1|I2C1_CLK -> Net-(R793-Pad2)
- U704 pad 14: GPIO1|I2C1_CLK -> Net-(R794-Pad2)
- U704 pad 4: SENSOR_INT1 -> Net-(R732-Pad2)
- U704 pad 9: SENSOR_INT2 -> Net-(R733-Pad2)
